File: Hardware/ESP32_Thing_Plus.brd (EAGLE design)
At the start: 22.9 x 58.4 mm, 104 parts, among them J1 AMP FCI 10103594-0001LF, Q1 2.5A/30V, Q2 MBT3904DW1T1, U1 MCP73831, U2 ESP-WROOM-32NARROW, U3 AP2112K-3.3V, U4 CP2102N

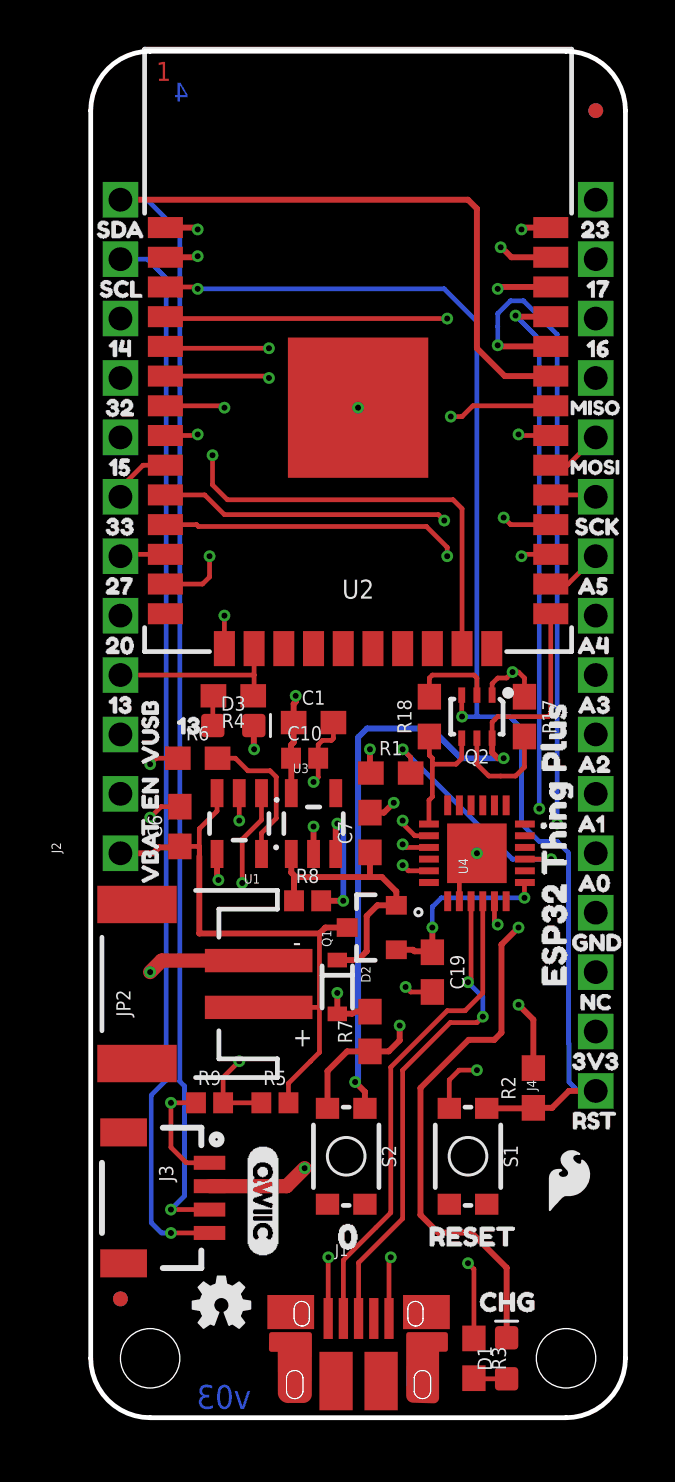
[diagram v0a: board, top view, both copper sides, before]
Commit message: V03 Changes Cont.
- Removed battery voltage divider
- Increased Board name silk on bottom
- Added NC buzzard labels to unconnected header pin.
- Added button to GPIO-0
- Swapped battery pins to match lipo battery pins
- Fixed missing pin connections on USB transceiver.
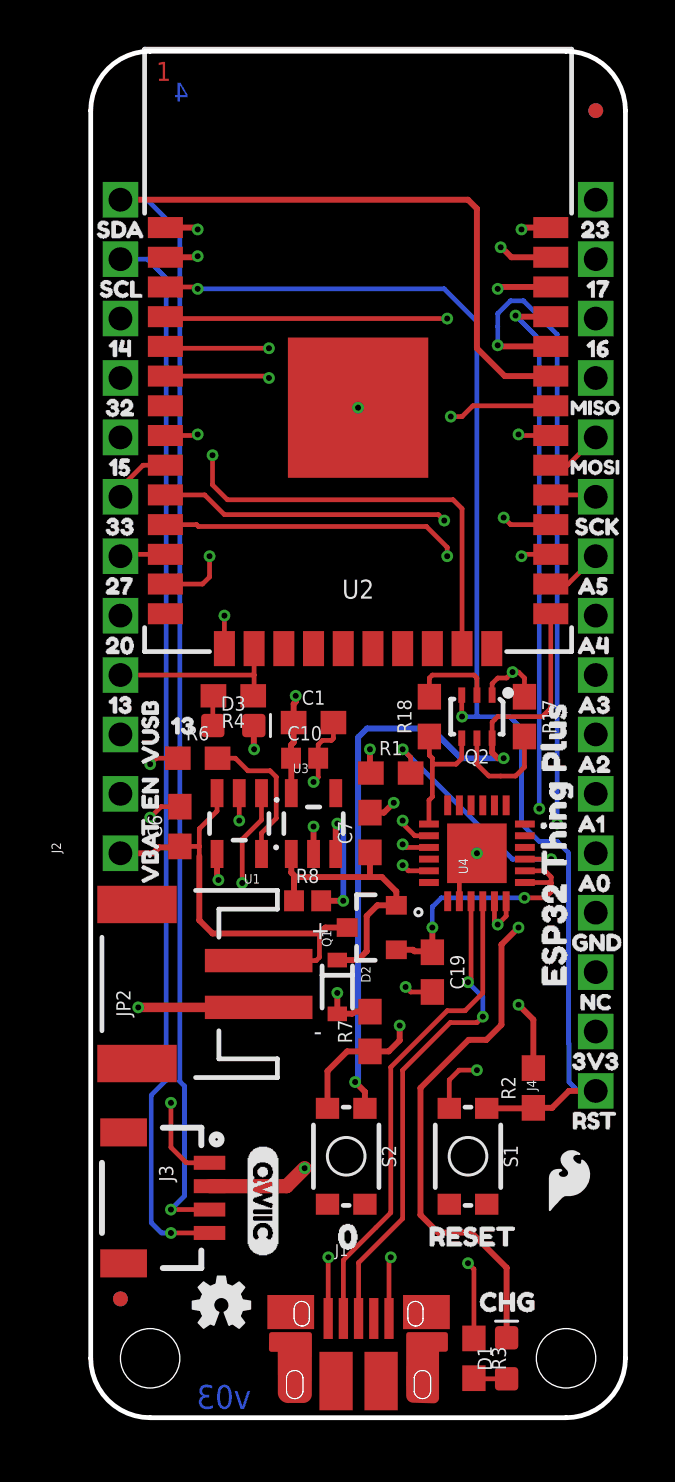
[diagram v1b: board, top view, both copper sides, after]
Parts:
- removed R5, R9: 100K, SparkFun-Resistors:0402
- removed U$61: (no value), buzzard_labels (43):ESP32_THING_PLUS0
- added U$64: (no value), buzzard_labels:NC0
- added U$65: (no value), buzzard_labels:ESP32_THING_PLUS0
- moved U$53 0.25 mm to (2.79, 29.6)
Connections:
- removed net VDD: U4.6
- net 3.3V: now also U4.6
- net 35: no longer R5.1, R9.2
- net GND: now also JP2.1; no longer JP2.2, R9.1
- net V_BATT: now also JP2.2; no longer JP2.1, R5.2
- net V_USB: now also U4.8
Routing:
- net 35: track 36.3 -> 0.00 mm, vias 2 -> 0
- net V_BATT: track 26.9 -> 19.6 mm
- net V_USB: track 17.7 -> 21.3 mm
- net 3.3V: track 24.7 -> 25.9 mm
- net GND: track 38.9 -> 38.2 mm

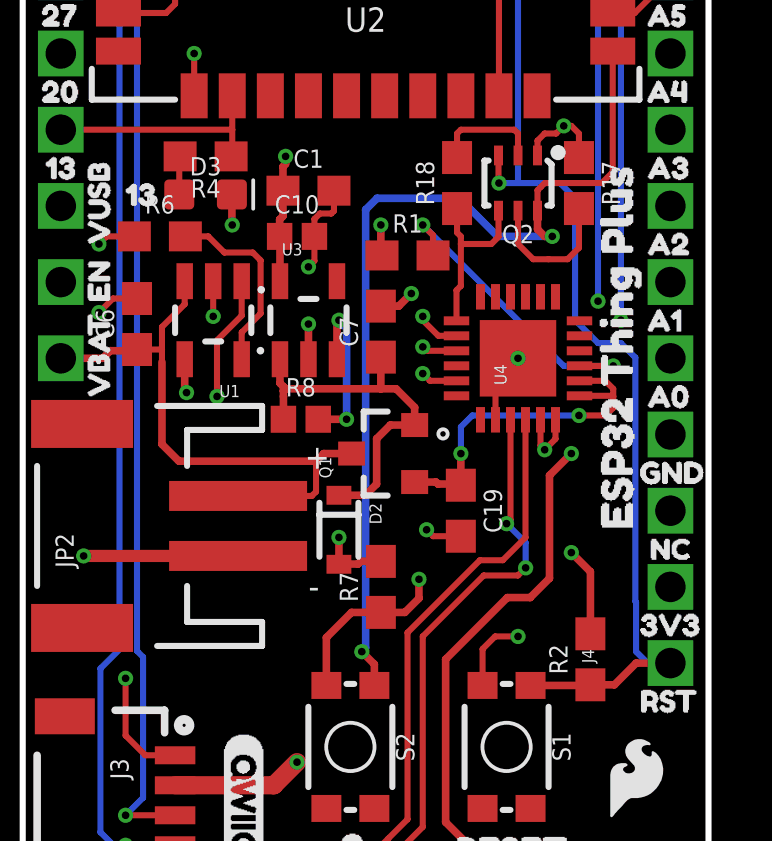
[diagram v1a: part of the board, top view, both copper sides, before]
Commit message: V03 QC Fixes
- Replaced via on GPIO0 with test point via
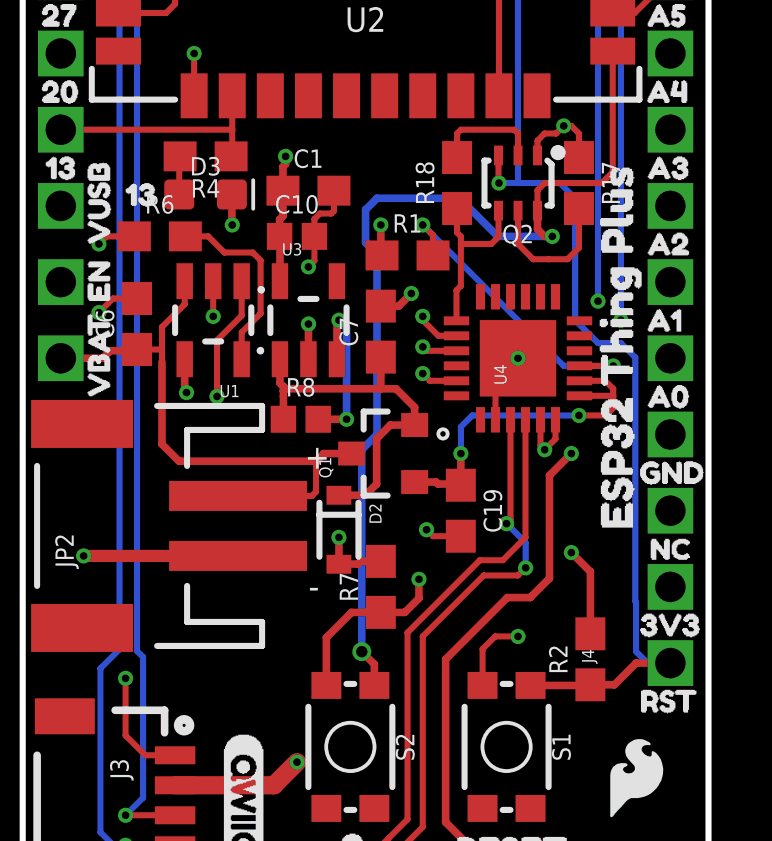
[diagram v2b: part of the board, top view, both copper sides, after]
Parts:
- added TP1: (no value), SparkFun-Connectors:TP_15TH
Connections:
- net 0: now also TP1.P$1
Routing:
- net 0: track 31.7 -> 32.0 mm, vias 2 -> 1
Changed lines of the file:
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@@
 <layers>
 <layer number="1" name="Top" color="4" fill="1" visible="yes" active="yes"/>
-<layer number="2" name="Route2" color="1" fill="3" visible="yes" active="yes"/>
-<layer number="15" name="Route15" color="4" fill="6" visible="yes" active="yes"/>
-<layer number="16" name="Bottom" color="1" fill="1" visible="yes" active="yes"/>
+<layer number="2" name="Route2" color="1" fill="3" visible="no" active="yes"/>
+<layer number="15" name="Route15" color="4" fill="6" visible="no" active="yes"/>
+<layer number="16" name="Bottom" color="1" fill="1" visible="no" active="yes"/>
 <layer number="17" name="Pads" color="2" fill="1" visible="yes" active="yes"/>
 <layer number="18" name="Vias" color="2" fill="1" visible="yes" active="yes"/>
 <layer number="19" name="Unrouted" color="6" fill="1" visible="yes" active="yes"/>
 <layer number="20" name="Dimension" color="15" fill="1" visible="yes" active="yes"/>
-<layer number="21" name="tPlace" color="16" fill="1" visible="no" active="yes"/>
-<layer number="22" name="bPlace" color="14" fill="1" visible="yes" active="yes"/>
+<layer number="21" name="tPlace" color="16" fill="1" visible="yes" active="yes"/>
+<layer number="22" name="bPlace" color="14" fill="1" visible="no" active="yes"/>
 <layer number="23" name="tOrigins" color="15" fill="1" visible="yes" active="yes"/>
 <layer number="24" name="bOrigins" color="15" fill="1" visible="yes" active="yes"/>
@@
 <layer number="27" name="tValues" color="7" fill="1" visible="no" active="yes"/>
 <layer number="28" name="bValues" color="7" fill="1" visible="no" active="yes"/>
-<layer number="29" name="tStop" color="7" fill="3" visible="no" active="yes"/>
+<layer number="29" name="tStop" color="7" fill="3" visible="yes" active="yes"/>
 <layer number="30" name="bStop" color="7" fill="6" visible="no" active="yes"/>
 <layer number="31" name="tCream" color="7" fill="4" visible="no" active="yes"/>
@@
 <element name="U$64" library="buzzard_labels" package="NC0" value="" x="21.209" y="19.05" rot="MR0"/>
 <element name="U$65" library="buzzard_labels" package="ESP32_THING_PLUS0" value="" x="11.43" y="43.18" rot="MR270"/>
+<element name="TP1" library="SparkFun-Connectors" package="TP_15TH" value="" x="11.303" y="14.351"/>
 </elements>
 <signals>
@@
 <wire x1="19.668" y1="30.336" x2="19.668" y2="34.37" width="0.2032" layer="1"/>
 <contactref element="S2" pad="4"/>
-<wire x1="17.272" y1="29.845" x2="17.399" y2="29.972" width="0.2032" layer="1"/>
-<wire x1="17.272" y1="29.845" x2="17.16" y2="29.733" width="0.2032" layer="1"/>
+<wire x1="17.16" y1="29.733" x2="17.399" y2="29.972" width="0.2032" layer="1"/>
 <wire x1="17.16" y1="29.733" x2="17.16" y2="29.052" width="0.2032" layer="1"/>
 <wire x1="11.722" y1="13.226" x2="11.722" y2="13.932" width="0.254" layer="1"/>
 <wire x1="11.722" y1="13.932" x2="11.303" y2="14.351" width="0.254" layer="1"/>
-<via x="11.303" y="14.351" extent="1-16" drill="0.254"/>
-<wire x1="11.43" y1="14.478" x2="11.43" y2="29.083" width="0.254" layer="16"/>
 <wire x1="11.43" y1="29.083" x2="11.811" y2="29.464" width="0.254" layer="16"/>
 <wire x1="11.811" y1="29.464" x2="14.561425" y2="29.464" width="0.254" layer="16"/>
@@
 <wire x1="17.399" y1="28.194" x2="17.16" y2="28.433" width="0.254" layer="1"/>
 <wire x1="17.16" y1="28.433" x2="17.16" y2="29.052" width="0.254" layer="1"/>
-<wire x1="11.303" y1="14.351" x2="11.43" y2="14.478" width="0.254" layer="16"/>
+<contactref element="TP1" pad="P$1"/>
+<wire x1="11.303" y1="14.351" x2="11.303" y2="21.082" width="0.254" layer="16"/>
+<wire x1="11.303" y1="21.082" x2="11.811" y2="21.59" width="0.254" layer="16"/>
+<wire x1="11.811" y1="21.59" x2="11.811" y2="27.602575" width="0.254" layer="16"/>
+<wire x1="11.811" y1="27.602575" x2="11.43" y2="27.983575" width="0.254" layer="16"/>
+<wire x1="11.43" y1="27.983575" x2="11.43" y2="29.083" width="0.254" layer="16"/>
 </signal>
 <signal name="N$17">

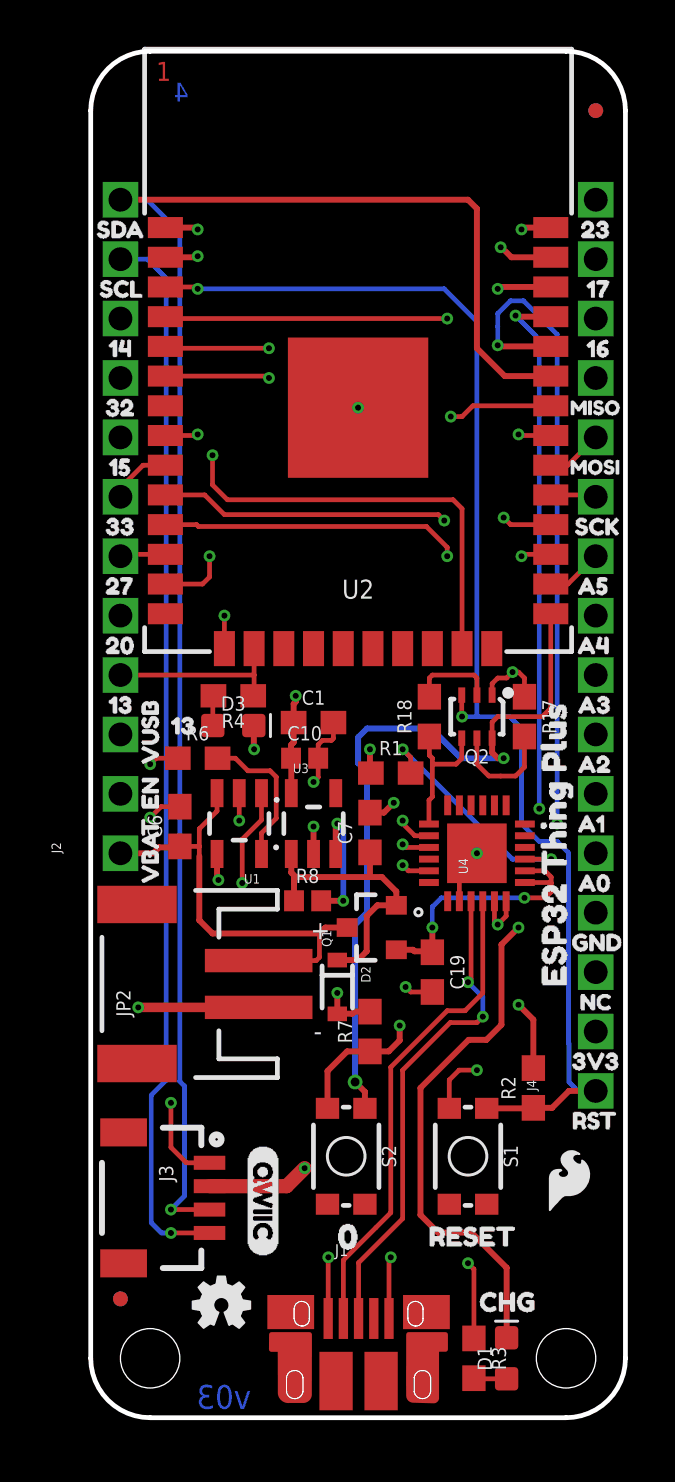
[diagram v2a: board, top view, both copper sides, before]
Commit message: v10
-Updated silk to include pin numbers and seondary functions for SPI/I2C/UART
-Remapped a couple outer pins to match board definitions file
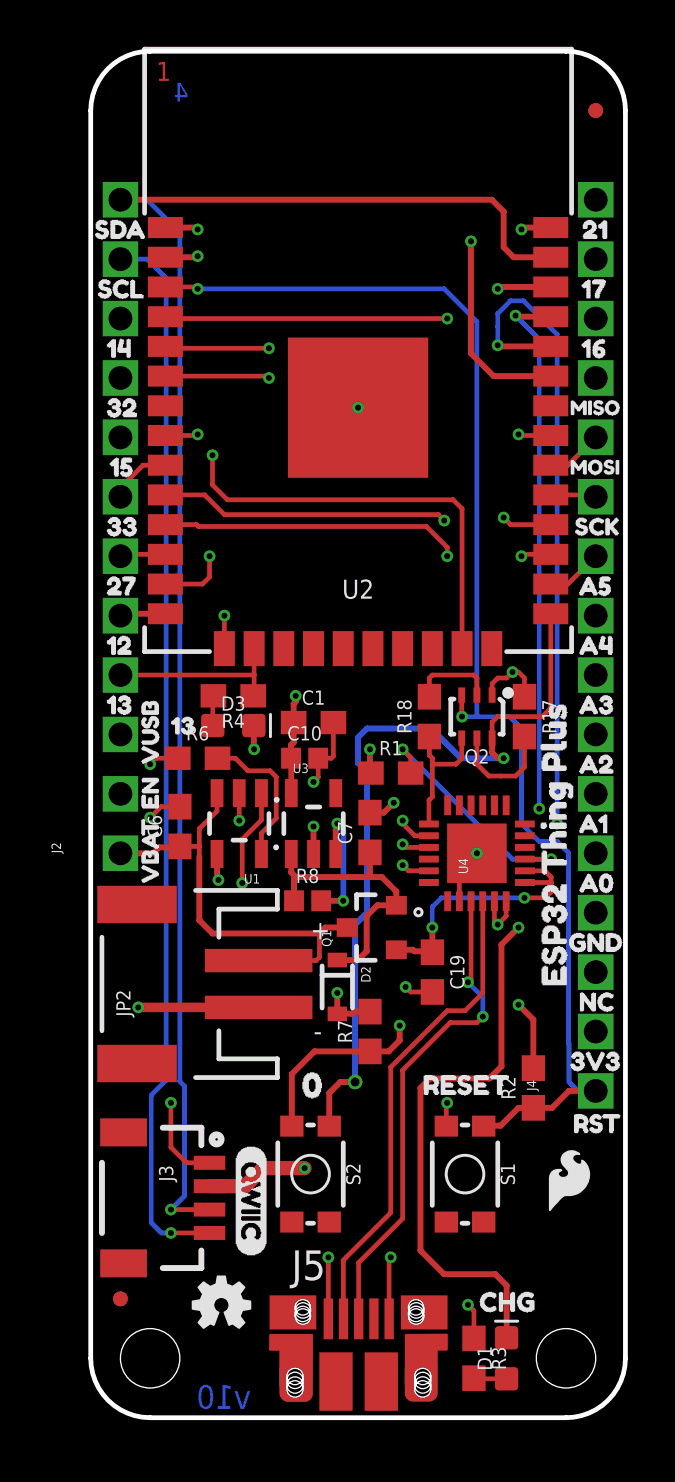
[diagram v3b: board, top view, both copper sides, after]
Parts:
- removed J1: AMP FCI 10103594-0001LF, SparkFun-Connectors:USB-MICROB-PTH-MILL
- removed U$21: (no value), buzzard_labels (37):MISO11
- removed U$22: (no value), buzzard_labels (37):MOSI10
- removed U$24: (no value), buzzard_labels (37):SCK9
- removed U$25: (no value), buzzard_labels (37):SCL16
- removed U$26: (no value), buzzard_labels (37):SDA15
- added J5: (no value), SparkFun-Connectors:USB-MICROB-PTH
- added U$61: (no value), buzzard_labels (4):RST24
- added U$66: (no value), buzzard_labels (5):18#MOSI1
- added U$67: (no value), buzzard_labels (5):19#MISO0
- added U$68: (no value), buzzard_labels (6):SCL#220
- added U$69: (no value), buzzard_labels (6):SDA#231
- U$29: device buzzard_labels (38):SDA0 -> buzzard_labels (4):SDA1
- U$30: device buzzard_labels (39):3V312 -> buzzard_labels (4):SCL0
- U$31: device buzzard_labels (39):137 -> buzzard_labels (4):142
- U$32: device buzzard_labels (39):141 -> buzzard_labels (4):323
- U$33: device buzzard_labels (39):153 -> buzzard_labels (4):154
- U$34: device buzzard_labels (39):206 -> buzzard_labels (4):335
- U$35: device buzzard_labels (39):275 -> buzzard_labels (4):276
- U$36: device buzzard_labels (39):322 -> buzzard_labels (4):127
- U$37: device buzzard_labels (39):334 -> buzzard_labels (4):138
- U$38: device buzzard_labels (39):1623 -> buzzard_labels (4):219
- U$39: device buzzard_labels (39):1724 -> buzzard_labels (4):1710
- U$40: device buzzard_labels (39):2325 -> buzzard_labels (4):1611
- U$41: device buzzard_labels (39):A014 -> buzzard_labels (4):A515
- U$42: device buzzard_labels (39):A115 -> buzzard_labels (4):A416
- U$43: device buzzard_labels (39):A216 -> buzzard_labels (4):A317
- U$44: device buzzard_labels (39):A317 -> buzzard_labels (4):A218
- U$45: device buzzard_labels (39):A418 -> buzzard_labels (4):A119
- U$46: device buzzard_labels (39):A519 -> buzzard_labels (4):A020
- U$48: device buzzard_labels (39):RST11 -> buzzard_labels (4):GND21
- U$49: device buzzard_labels (39):GND13 -> buzzard_labels (4):NC22
- U$6: device buzzard_labels (37):1612 -> buzzard_labels (7):16#RX11
- U$60: device buzzard_labels (39):SCL0 -> buzzard_labels (4):3V323
- U$63: device buzzard_labels:NC1 -> buzzard_labels (5):5#SCK2
- U$7: device buzzard_labels (37):1713 -> buzzard_labels (7):17#TX10
- moved U$30 38.8 mm to (-0.38, 48.3)
- moved U$60 38.6 mm to (19.8, 15.2)
- moved U$63 21.6 mm to (21.2, 39.4), flipped to the bottom
- moved U$31 15.2 mm to (0.00, 45.7)
- moved U$41 12.7 mm to (20.2, 35.6)
- moved U$46 12.7 mm to (20.2, 22.9)
- moved U$36 10.2 mm to (0.00, 33.0)
- moved U$48 7.62 mm to (19.8, 20.3)
- moved U$42 7.62 mm to (20.1, 33.0)
- moved U$45 7.62 mm to (20.2, 25.4)
- moved U$37 7.62 mm to (0.00, 30.5)
- moved U$62 6.65 mm to (8.13, 14.2)
- moved U$57 6.48 mm to (13.5, 14.2)
- moved U$38 5.09 mm to (20.2, 50.8)
- moved U$34 5.08 mm to (0.00, 38.1)
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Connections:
- removed net 23: J4.16, U2.37
- new net 21: J4.16, U2.33
- net 12: now also J2.5
- net 20: no longer J2.5
- net D+: now also J5.D+; no longer J1.D+
- net D-: now also J5.D-; no longer J1.D-
- net GND: now also J5.GND; no longer J1.GND
- net SDA: now also U2.37; no longer U2.33
- net V_USB: now also J5.VBUS; no longer J1.VBUS
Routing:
- net 20: track 22.7 -> 0.00 mm, vias 1 -> 0
- net 21: track 0.00 -> 15.0 mm, vias 0 -> 1
- net 23: track 7.22 -> 0.00 mm, vias 1 -> 0
- net SDA: track 71.9 -> 67.2 mm
- net 12: track 0.00 -> 1.96 mm
- net V_USB: track 21.3 -> 19.5 mm
- net CHG: track 40.2 -> 41.7 mm
- net 0: track 32.0 -> 33.4 mm
- net GND: track 38.2 -> 39.0 mm
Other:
- board text added: "v10"
- board text removed: "v03"
